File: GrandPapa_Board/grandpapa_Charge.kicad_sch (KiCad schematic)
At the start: 22 parts

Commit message: fix erc
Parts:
- gave numbers to parts that had none: 22

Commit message: fix SHDN pin config on 4.5V regulator
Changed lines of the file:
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@@
 (kicad_sch (version 20211123) (generator eeschema)
   (paper "A4")
-  (junction (at 50.8 62.23) (diameter 0) (color 0 0 0 0)
-  )
   (junction (at 200.66 69.85) (diameter 0) (color 0 0 0 0)
   )
@@
     (stroke (width 0) (type default) (color 0 0 0 0))
   )
-  (wire (pts (xy 54.61 52.705) (xy 50.8 52.705))
-    (stroke (width 0) (type default) (color 0 0 0 0))
-  )
   (wire (pts (xy 200.66 69.85) (xy 204.47 69.85))
     (stroke (width 0) (type default) (color 0 0 0 0))
   )
+  (wire (pts (xy 109.22 124.46) (xy 118.745 124.46))
+    (stroke (width 0) (type default) (color 0 0 0 0))
+  )
   (wire (pts (xy 126.365 115.57) (xy 126.365 106.045))
     (stroke (width 0) (type default) (color 0 0 0 0))
@@
     (stroke (width 0) (type default) (color 0 0 0 0))
   )
+  (wire (pts (xy 109.22 124.46) (xy 109.22 123.19))
+    (stroke (width 0) (type default) (color 0 0 0 0))
+  )
   (polyline (pts (xy 191.77 139.065) (xy 151.13 139.065))
     (stroke (width 0) (type default) (color 0 0 0 0))
@@
     (stroke (width 0) (type default) (color 0 0 0 0))
   )
-  (wire (pts (xy 50.8 62.23) (xy 34.925 62.23))
+  (wire (pts (xy 34.925 62.23) (xy 57.785 62.23))
     (stroke (width 0) (type default) (color 0 0 0 0))
   )
@@
     (stroke (width 0) (type default) (color 0 0 0 0))
   )
-  (wire (pts (xy 114.3 123.19) (xy 113.03 123.19))
-    (stroke (width 0) (type default) (color 0 0 0 0))
-  )
   (polyline (pts (xy 150.495 104.775) (xy 191.77 104.775))
     (stroke (width 0) (type default) (color 0 0 0 0))
@@
     (stroke (width 0) (type default) (color 0 0 0 0))
   )
-  (wire (pts (xy 50.8 52.705) (xy 50.8 62.23))
-    (stroke (width 0) (type default) (color 0 0 0 0))
-  )
   (wire (pts (xy 69.85 66.675) (xy 72.39 66.675))
     (stroke (width 0) (type default) (color 0 0 0 0))
@@
     (stroke (width 0) (type default) (color 0 0 0 0))
   )
-  (wire (pts (xy 50.8 62.23) (xy 57.785 62.23))
-    (stroke (width 0) (type default) (color 0 0 0 0))
-  )
   (wire (pts (xy 72.39 80.645) (xy 73.66 80.645))
     (stroke (width 0) (type default) (color 0 0 0 0))
@@
     (stroke (width 0) (type default) (color 0 0 0 0))
   )
-  (wire (pts (xy 114.3 124.46) (xy 114.3 123.19))
-    (stroke (width 0) (type default) (color 0 0 0 0))
-  )
   (wire (pts (xy 164.465 88.265) (xy 164.465 115.57))
     (stroke (width 0) (type default) (color 0 0 0 0))
@@
   )
   (wire (pts (xy 38.1 90.805) (xy 73.66 90.805))
-    (stroke (width 0) (type default) (color 0 0 0 0))
-  )
-  (wire (pts (xy 118.745 124.46) (xy 114.3 124.46))
     (stroke (width 0) (type default) (color 0 0 0 0))
   )
@@
   (text "VBATT_CURR_SENSE = Iout*R3*100V/V = (5V-0.02V) max = 4.98V max\nI_max_sense = (4.98V)/(20mR*100V/V) = 2.49A"
     (at 186.69 60.96 0)
-    (effects (font (size 1.27 1.27)) (justify left bottom))
-  )
-  (label "+4.5V_MCP73871" (at 113.03 123.19 180)
-    (effects (font (size 1.27 1.27)) (justify right bottom))
-  )
-  (label "+4.5V_MCP73871" (at 54.61 52.705 0)
     (effects (font (size 1.27 1.27)) (justify left bottom))
   )
@@
       (effects (font (size 1.27 1.27)) hide)
     )
+    (pin "1")
+  )
+  (symbol (lib_id "grandpapa board:+4.5V") (at 109.22 120.65 0) (unit 1)
+    (in_bom yes) (on_board yes)
+    (property "Reference" "#PWR?" (id 0) (at 109.22 117.475 0)
+      (effects (font (size 1.27 1.27)) hide)
+    )
+    (property "Value" "+4.5V" (id 1) (at 109.22 118.11 0))
+    (property "Footprint" "" (id 2) (at 115.57 119.38 0)
+      (effects (font (size 1.27 1.27)) hide)
+    )
+    (property "Datasheet" "" (id 3) (at 115.57 119.38 0)
+      (effects (font (size 1.27 1.27)) hide)
+    )

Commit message: Addressed some Jack comments. 3/4/6/7 TBD
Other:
- moved on the sheet: C11, J1, R22, TP1, TP2

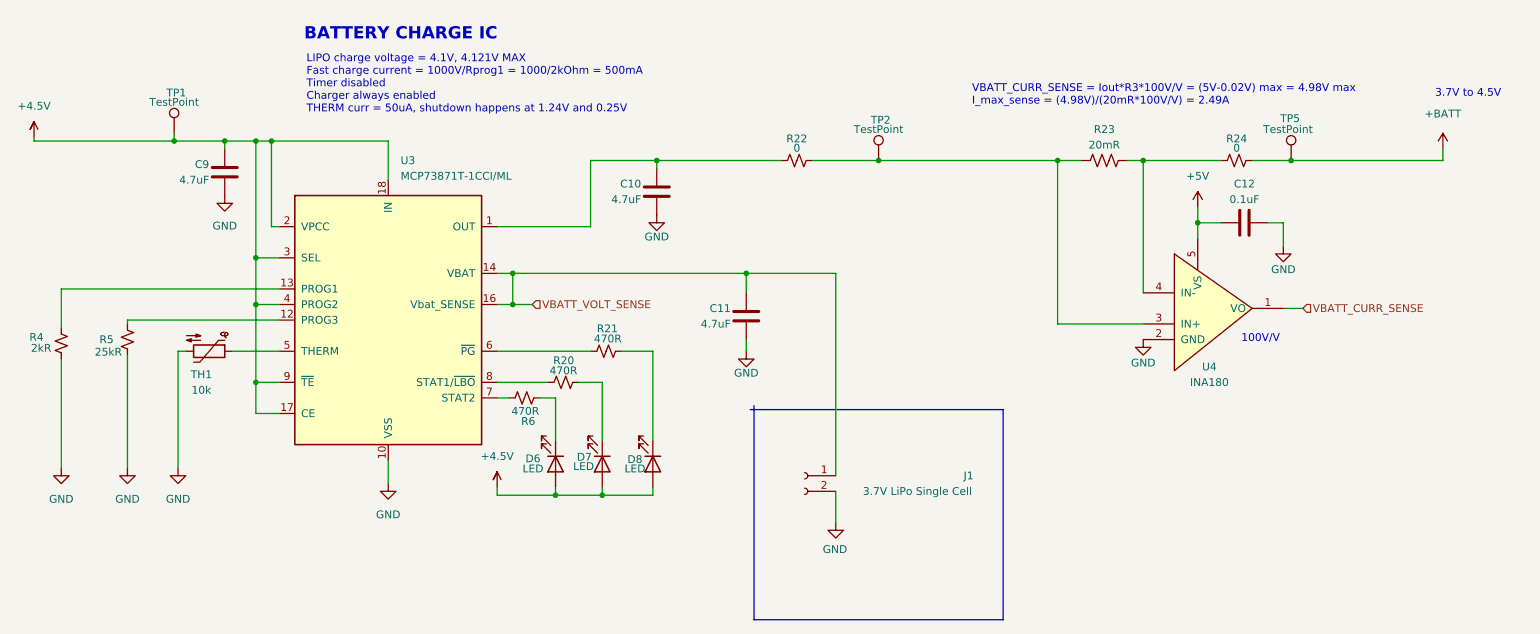
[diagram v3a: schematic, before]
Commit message: address the rest of jack's review, still need to fix grid spacing
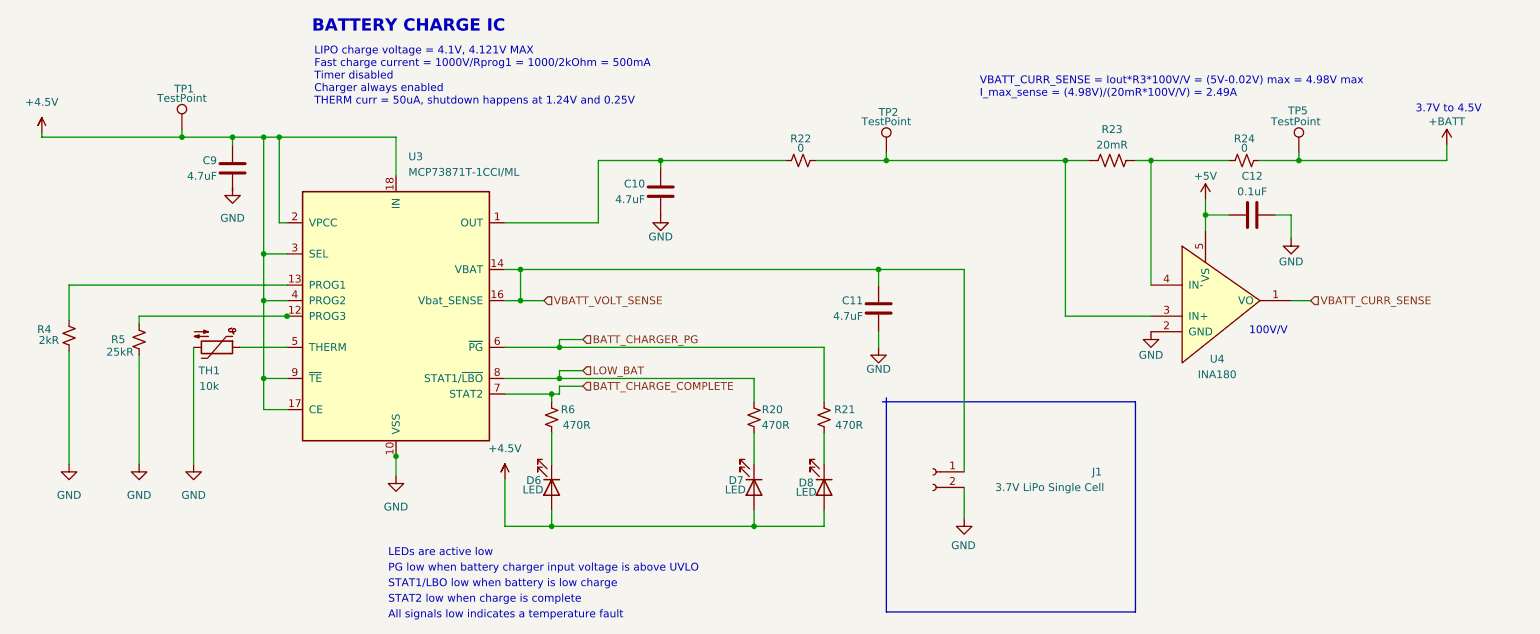
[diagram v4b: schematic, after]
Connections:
- net GND: no longer C9.2
- net at R21.1: now also D8.1 (K); no longer U3.6 (~{PG})
- net BATT_CHARGER_PG: now reaches R21.2
- net BATT_CHARGER_PG: now also U3.6 (~{PG}); no longer D8.1 (K)
- net at R6.1: now also D6.1 (K); no longer U3.7 (STAT2)
- net BATT_CHARGE_COMPLETE: now reaches R6.2
- net BATT_CHARGE_COMPLETE: now also U3.7 (STAT2); no longer D6.1 (K)
- net LOW_BAT: now reaches R20.1, U3.8 (STAT1/~{LBO})
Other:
- note added: "All signals low indicates a temperature fault"
- note added: "LEDs are active low"
- note added: "PG low when battery charger input voltage is above UVLO"
- note added: "STAT1/LBO low when battery is low charge"
- note added: "STAT2 low when charge is complete"
- moved on the sheet: C10, C11, C12, C9, D7, D8, J1, R20, R21, R22, R23, R24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

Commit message: fix disconnected pins, connect new hierarchical pins, misc layout changes
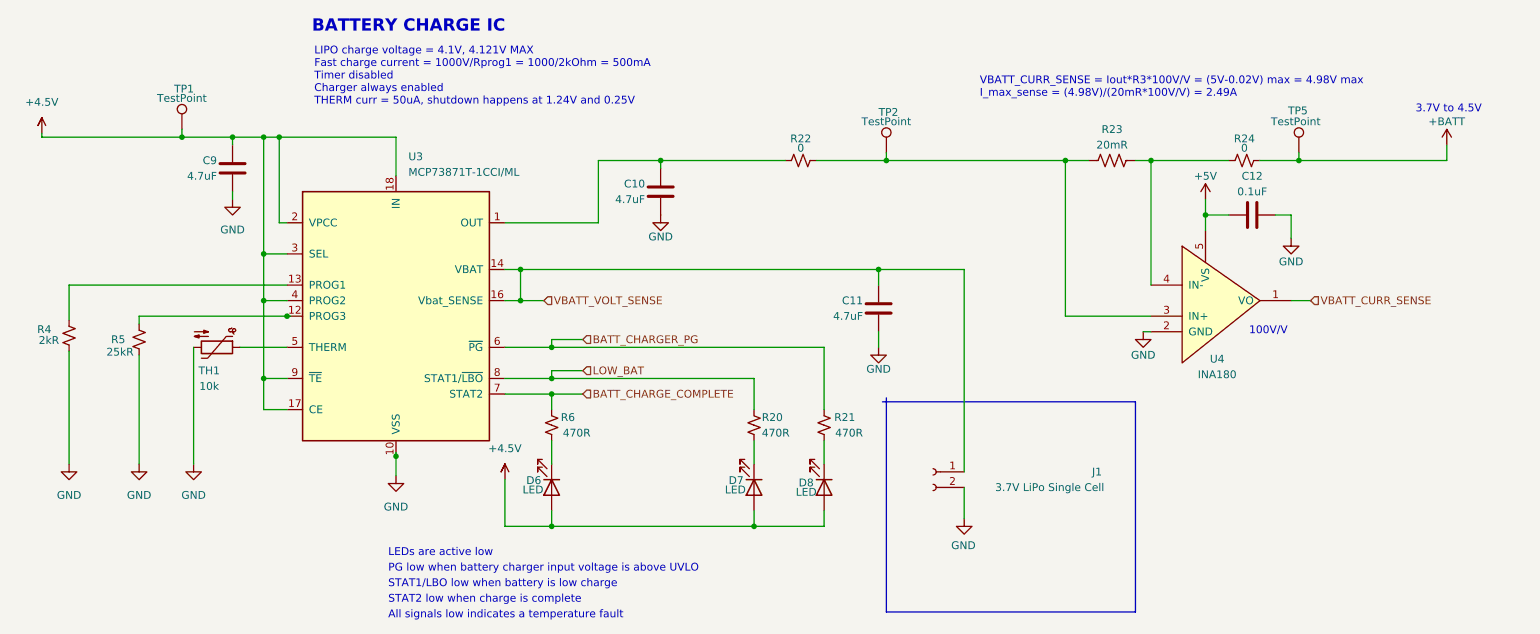
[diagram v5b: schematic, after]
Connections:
- net GND: now also C9.2
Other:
- moved on the sheet: R20, R21, R6

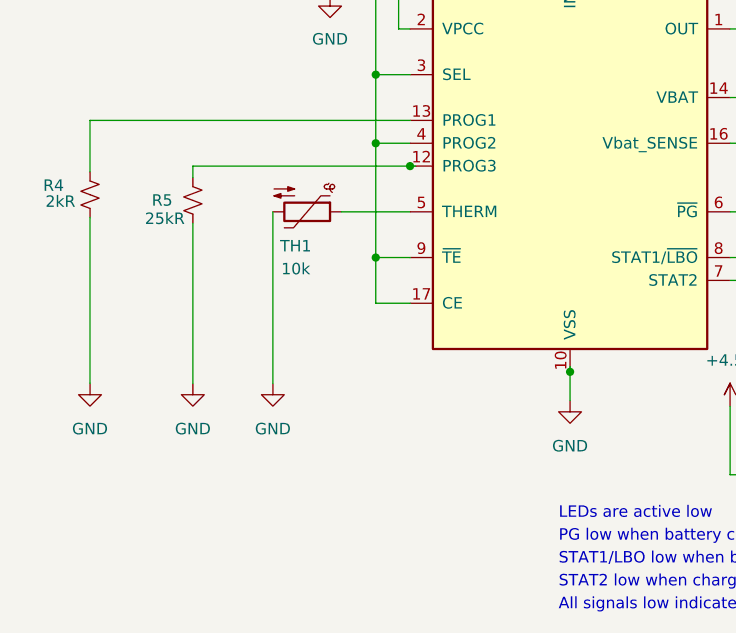
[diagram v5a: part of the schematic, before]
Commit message: minor fixes; chip shortage tearing me a new one
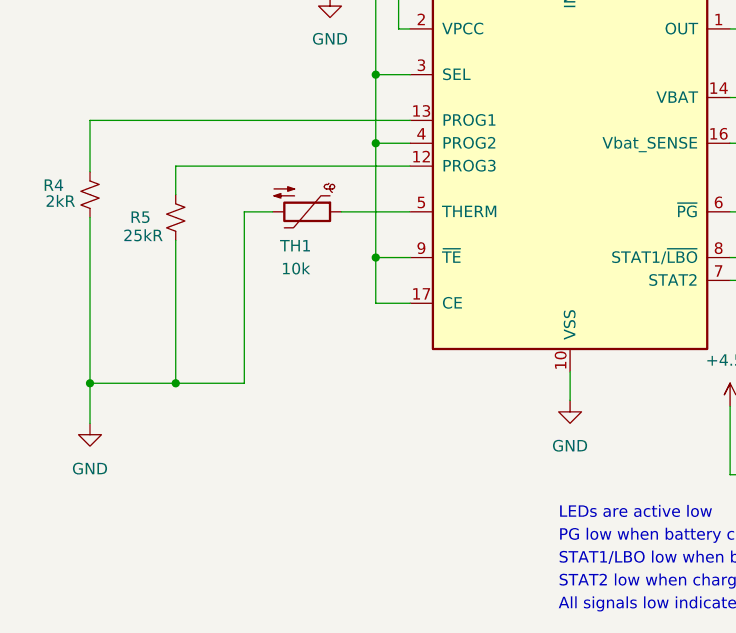
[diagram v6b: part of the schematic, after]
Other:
- moved on the sheet: R5
